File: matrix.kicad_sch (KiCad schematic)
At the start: 195 parts, among them SW10 ?, SW100 ?, SW101 ?, SW102 ?, SW103 ?, SW104 ?, SW105 ?, SW11 ?, SW12 ?, SW13 ?, SW14 ?, SW15 ?, SW16 ?, SW17 ?, SW18 ?, SW19 ?, SW2 ?, SW20 ?, SW21 ?, SW22 ?, SW23 ?, SW24 ?, SW25 ?, SW26 ?, SW27 ?, SW28 ?, SW29 ?, SW3 ?, SW30 ?, SW31 ?, SW32 ?, SW33 ?, SW34 ?, SW35 ?, SW36 ?, SW37 ?, SW38 ?, SW39 ?, SW4 ?, SW40 ?, SW41 ?, SW42 ?, SW43 ?, SW44 ?, SW45 ?, SW46 ?, SW47 ?, SW48 ?, SW49 ?, SW5 ?, SW50 ?, SW51 ?, SW52 ?, SW53 ?, SW54 ?, SW55 ?, SW56 ?, SW57 ?, SW58 ?, SW59 ?, SW6 ?, SW60 ?, SW61 ?, SW62 ?, SW63 ?, SW64 ?, SW65 ?, SW66 ?, SW67 ?, SW68 ?, SW69 ?, SW7 ?, SW70 ?, SW71 ?, SW72 ?, SW73 ?, SW74 ?, SW75 ?, SW76 ?, SW77 ?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

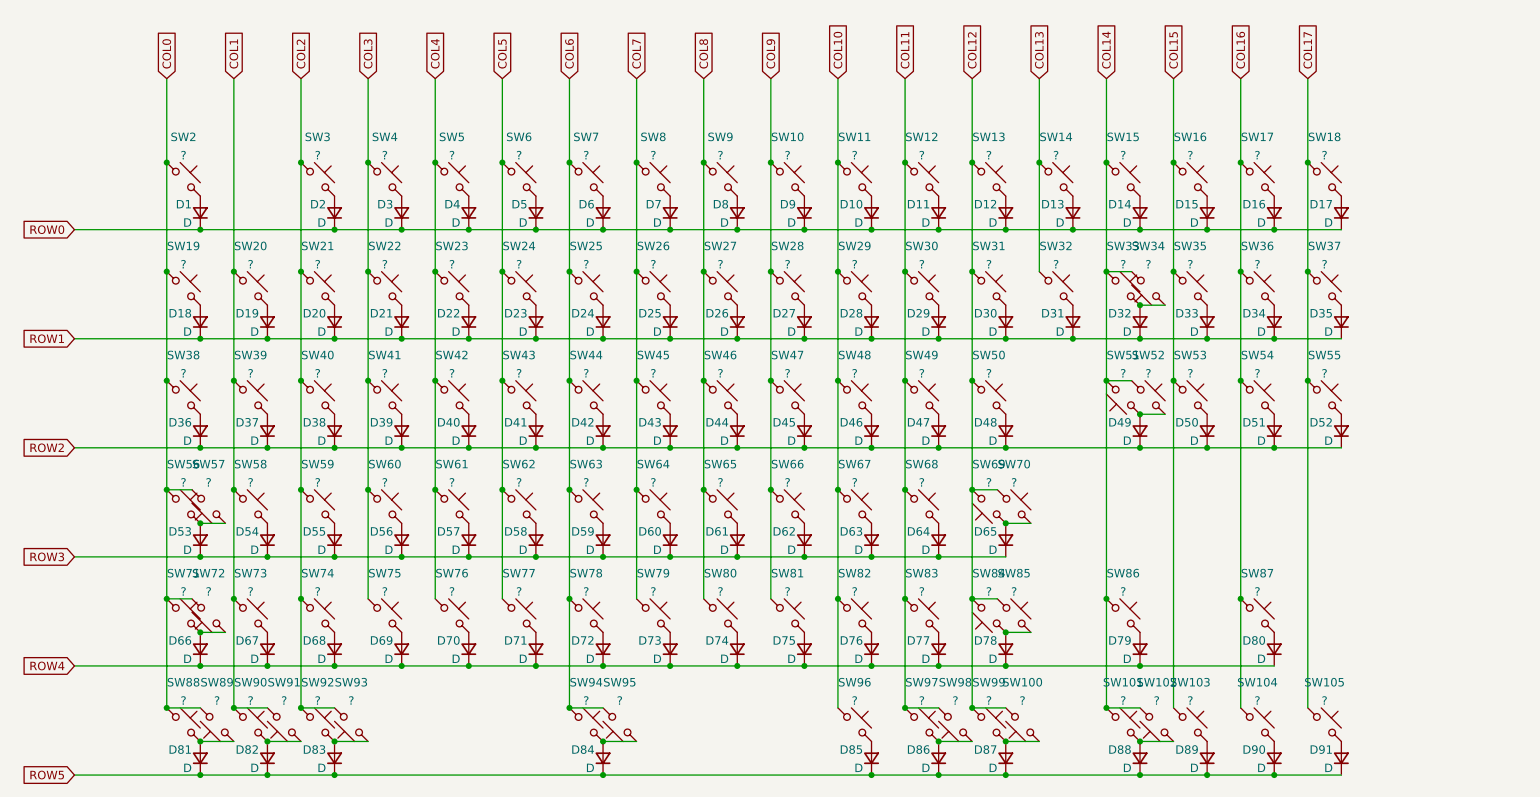
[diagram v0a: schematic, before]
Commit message: Added Stabilizers
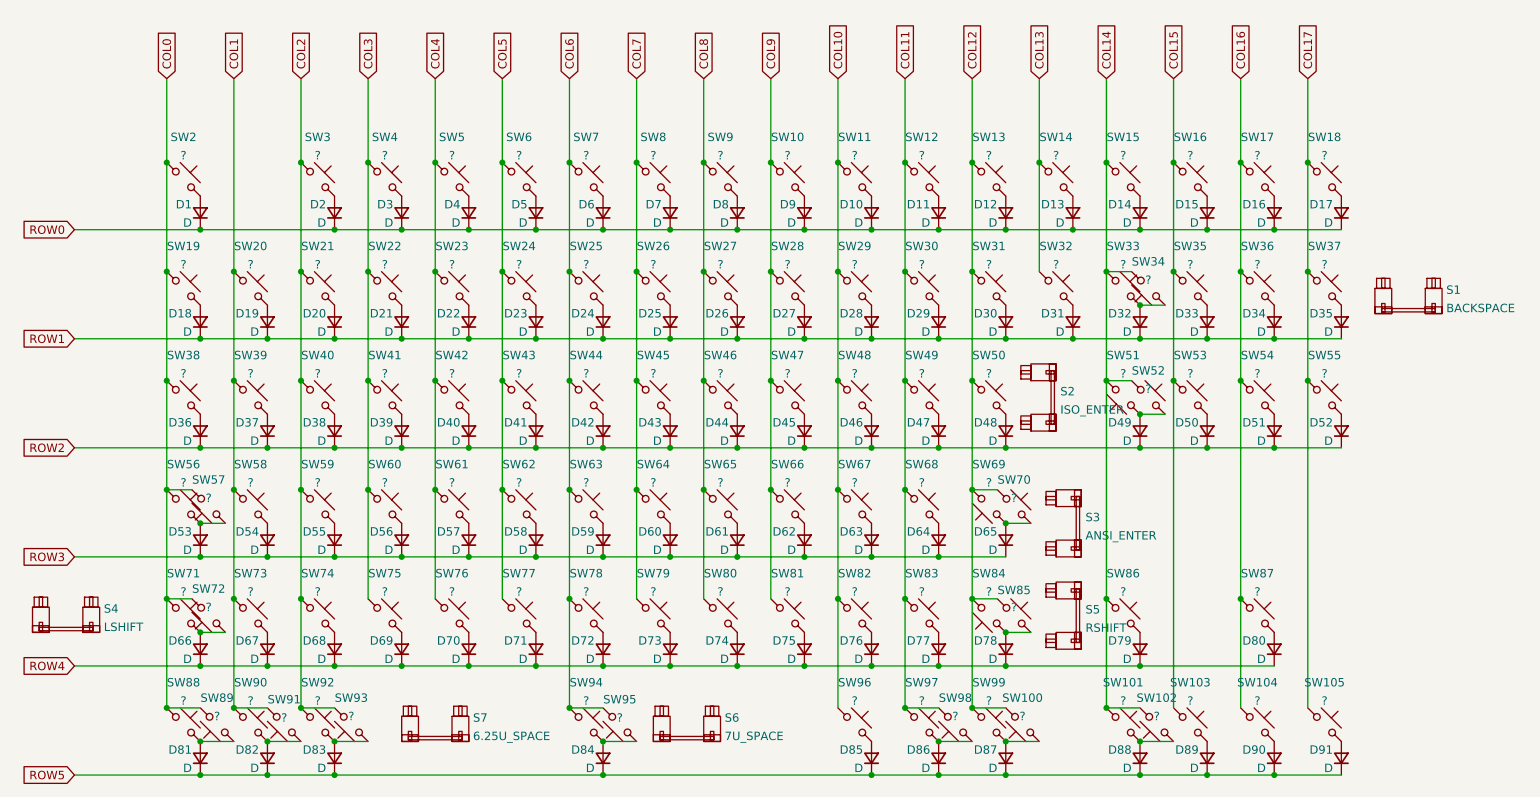
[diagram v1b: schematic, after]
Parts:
- added S1: BACKSPACE, marbastlib-mx:STAB_MX_2u, symbol marbastlib-mx:MX_stab
- added S2: ISO_ENTER, marbastlib-mx:STAB_MX_ISO_FLIPPED, symbol marbastlib-mx:MX_stab
- added S3: ANSI_ENTER, marbastlib-mx:STAB_MX_2.25u, symbol marbastlib-mx:MX_stab
- added S4: LSHIFT, marbastlib-mx:STAB_MX_2.25u, symbol marbastlib-mx:MX_stab
- added S5: RSHIFT, marbastlib-mx:STAB_MX_2.75u, symbol marbastlib-mx:MX_stab
- added S6: 7U_SPACE, marbastlib-mx:STAB_MX_7u, symbol marbastlib-mx:MX_stab
- added S7: 6.25U_SPACE, marbastlib-mx:STAB_MX_6.25u, symbol marbastlib-mx:MX_stab

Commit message: All switches (not diodes) in position
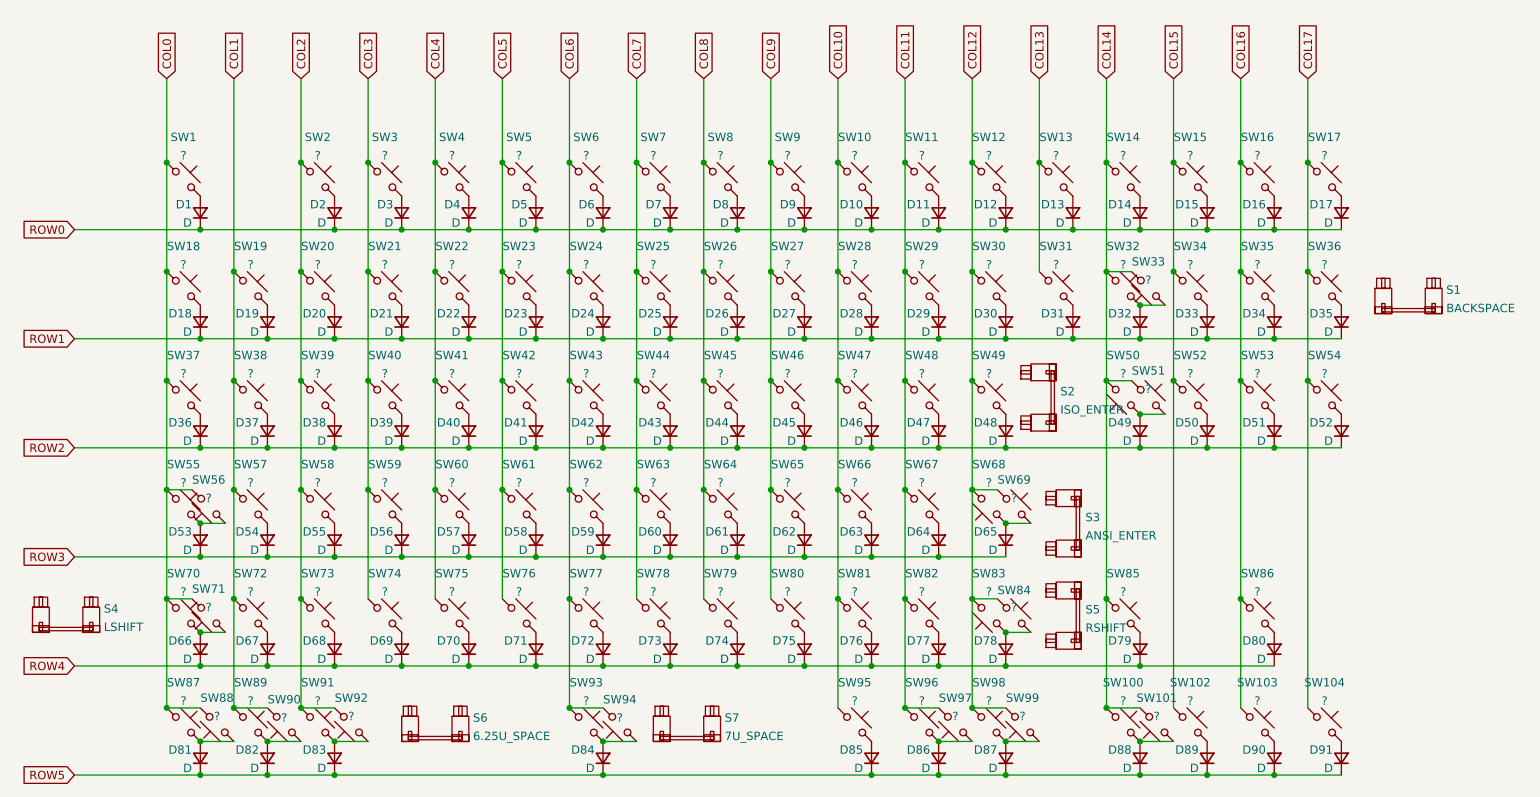
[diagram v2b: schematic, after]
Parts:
- renumbered S7 to S6, S6 to S7, SW2 to SW1, SW11 to SW10, SW101 to SW100, SW102 to SW101, SW103 to SW102, SW104 to SW103, SW105 to SW104, SW12 to SW11, SW13 to SW12, SW14 to SW13, SW15 to SW14, SW16 to SW15, SW17 to SW16, SW18 to SW17, SW19 to SW18, SW20 to SW19, SW3 to SW2, SW21 to SW20, SW22 to SW21, SW23 to SW22, SW24 to SW23, SW25 to SW24, SW26 to SW25, SW27 to SW26, SW28 to SW27, SW29 to SW28, SW30 to SW29, SW4 to SW3, SW31 to SW30, SW32 to SW31, SW33 to SW32, SW34 to SW33, SW35 to SW34, SW36 to SW35, SW37 to SW36, SW38 to SW37, SW39 to SW38, SW40 to SW39, SW5 to SW4, SW41 to SW40, SW42 to SW41, SW43 to SW42, SW44 to SW43, SW45 to SW44, SW46 to SW45, SW47 to SW46, SW48 to SW47, SW49 to SW48, SW50 to SW49, SW6 to SW5, SW51 to SW50, SW52 to SW51, SW53 to SW52, SW54 to SW53, SW55 to SW54, SW56 to SW55, SW57 to SW56, SW58 to SW57, SW59 to SW58, SW60 to SW59, SW7 to SW6, SW61 to SW60, SW62 to SW61, SW63 to SW62, SW64 to SW63, SW65 to SW64, SW66 to SW65, SW67 to SW66, SW68 to SW67, SW69 to SW68, SW70 to SW69, SW8 to SW7, SW71 to SW70, SW72 to SW71, SW73 to SW72, SW74 to SW73, SW75 to SW74, SW76 to SW75, SW77 to SW76, SW78 to SW77, SW79 to SW78, SW80 to SW79, SW9 to SW8, SW81 to SW80, SW82 to SW81, SW83 to SW82, SW84 to SW83, SW85 to SW84, SW86 to SW85, SW87 to SW86, SW88 to SW87, SW89 to SW88, SW90 to SW89, SW10 to SW9, SW91 to SW90, SW92 to SW91, SW93 to SW92, SW94 to SW93, SW95 to SW94, SW96 to SW95, SW97 to SW96, SW98 to SW97, SW99 to SW98, SW100 to SW99

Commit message: Changed Diodes to sod123
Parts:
- D1, D10, D11, D12, D13, D14, D15, D16, D17, D18, D19, D2, D20, D21, D22, D23, D24, D25, D26, D27, D28, D29, D3, D30, D31, D32, D33, D34, D35, D36, D37, D38, D39, D4, D40, D41, D42, D43, D44, D45, D46, D47, D48, D49, D5, D50, D51, D52, D53, D54, D55, D56, D57, D58, D59, D6, D60, D61, D62, D63, D64, D65, D66, D67, D68, D69, D7, D70, D71, D72, D73, D74, D75, D76, D77, D78, D79, D8, D80, D81, D82, D83, D84, D85, D86, D87, D88, D89, D9, D90, D91: footprint Diode_SMD:D_0402_1005Metric -> Diode_SMD:D_SOD-123
- SW100, SW37, SW50, SW88, SW92, SW96: footprint marbastlib-mx:SW_MX_HS_1u -> marbastlib-mx:SW_MX_HS_1.5u
- SW101, SW70, SW87, SW89, SW91, SW95, SW97, SW99: footprint marbastlib-mx:SW_MX_HS_1u -> marbastlib-mx:SW_MX_HS_1.25u
- SW55: footprint marbastlib-mx:SW_MX_HS_1u -> marbastlib-mx:SW_MX_HS_1.75u_stp
- SW56, SW83: footprint marbastlib-mx:SW_MX_HS_1u -> marbastlib-mx:SW_MX_HS_1.75u

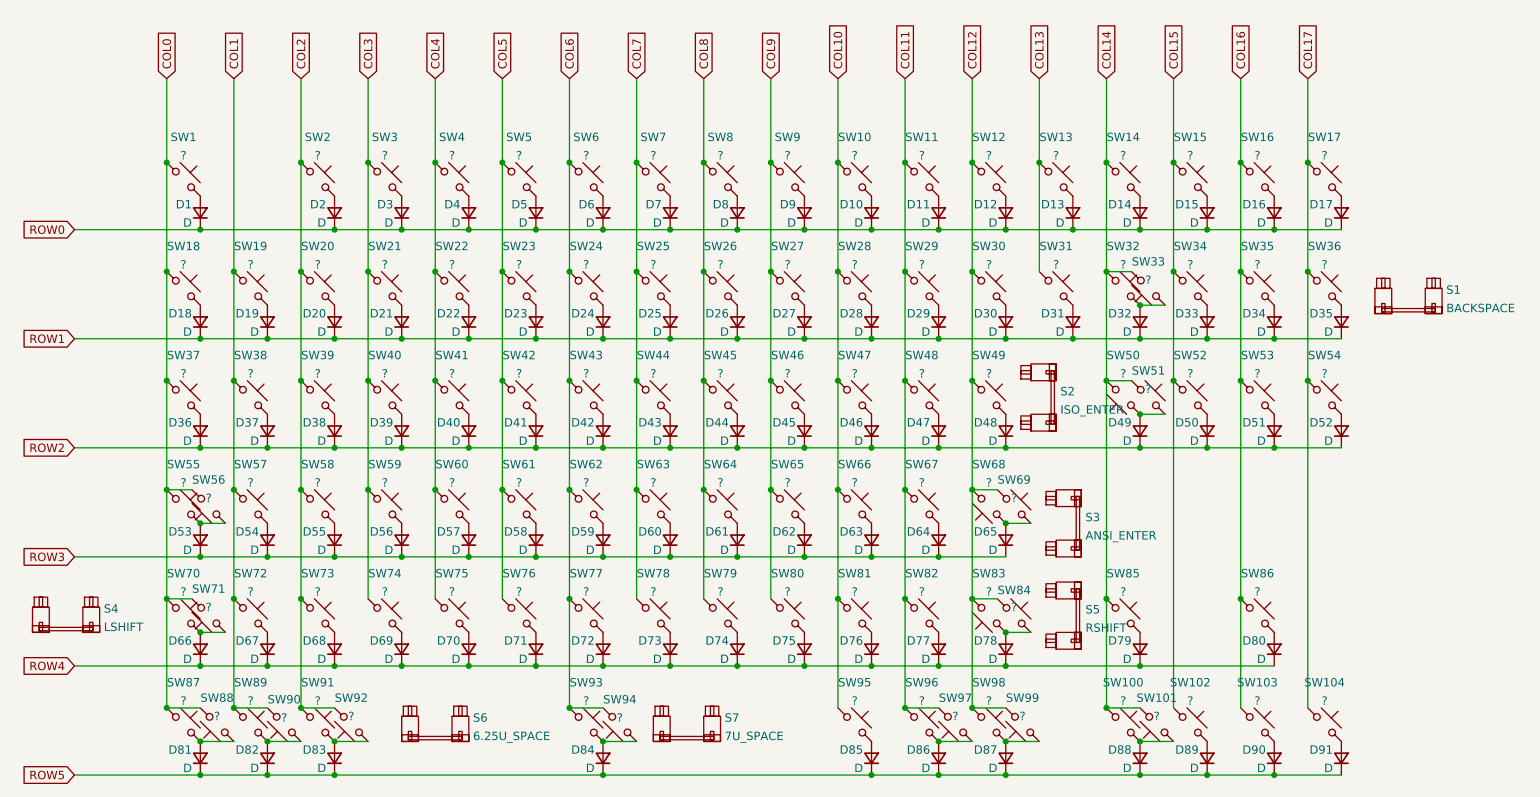
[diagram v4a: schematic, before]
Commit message: [Big changes] Added flex cuts and changed switch matrix/ pinout
- Optimized switch matrix by changing how the split backspace is done. It now connects to a different row instead of creating a whole different column
- Shifted a lot of traces/pins over by one, slight retracing work around the mcu area
- Added one more pin to the unused pins header
- Added 2 simple flex cuts
- Slight shifting around of different diodes
- Added 3d model for JST and USB-C Connector
- Extended bottom of the pcb by 0.5mm to accommodate for stab holes a bit better.
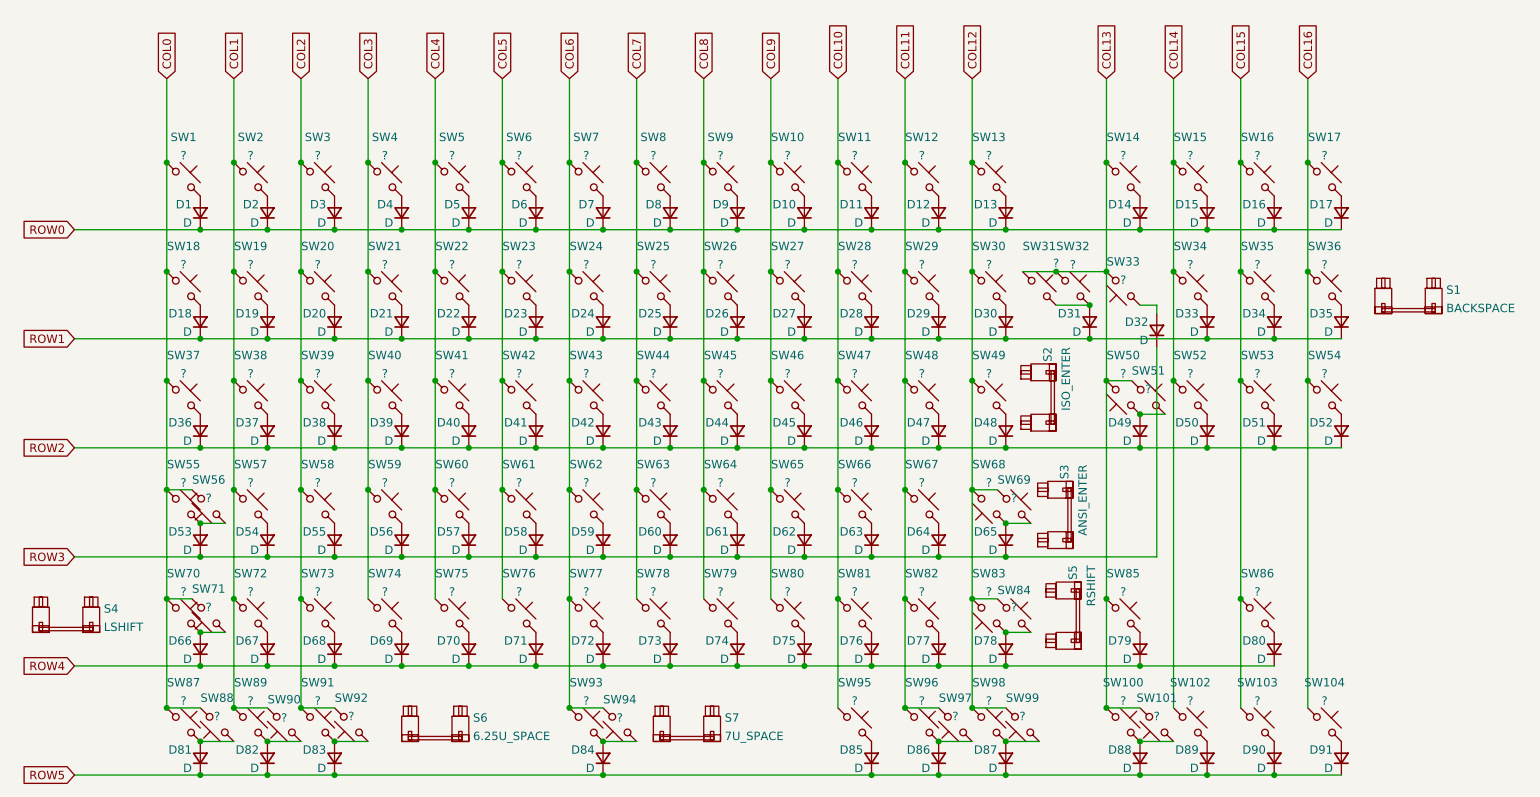
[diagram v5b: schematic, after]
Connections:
- net COL17 is gone; now on net COL16: SW104.1, SW17.1, SW36.1, SW54.1
- net COL1: now also SW2.1
- net COL10: now also SW11.1; no longer SW10.1
- net COL11: now also SW12.1; no longer SW11.1
- net COL12: now also SW13.1; no longer SW12.1
- net COL13: now also SW100.1, SW101.2, SW14.1, SW32.1, SW33.2, SW50.2, SW51.1, SW85.1; no longer SW13.1
- net COL14: now also SW102.1, SW15.1, SW34.1, SW52.1; no longer SW100.1, SW101.2, SW14.1, SW32.1, SW33.2, SW50.2, SW51.1, SW85.1
- net COL15: now also SW103.1, SW16.1, SW35.1, SW53.1, SW86.1; no longer SW102.1, SW15.1, SW34.1, SW52.1
- net COL16: no longer SW103.1, SW16.1, SW35.1, SW53.1, SW86.1
- net COL2: now also SW3.1; no longer SW2.1
- net COL3: now also SW4.1; no longer SW3.1
- net COL4: now also SW5.1; no longer SW4.1
- net COL5: now also SW6.1; no longer SW5.1
- net COL6: now also SW7.1; no longer SW6.1
- net COL7: now also SW8.1; no longer SW7.1
- net COL8: now also SW9.1; no longer SW8.1
- net COL9: now also SW10.1; no longer SW9.1
- net ROW1: no longer D32.1 (K)
- net ROW3: now also D32.1 (K)
- net at D31.2 (A), SW31.2: now also SW32.2
- net at D32.2 (A), SW33.1: no longer SW32.2
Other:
- moved on the sheet: D10, D11, D12, D13, D2, D3, D31, D32, D4, D5, D6, D7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

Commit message: Updated BOM inclusions
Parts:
- S1, S2, S3, S4, S5, S6, S7: now left out of the parts list
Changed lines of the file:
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@@
   )
   (symbol (lib_id "marbastlib-mx:MX_stab") (at 243.84 69.85 0) (unit 1)
-    (in_bom yes) (on_board yes) (fields_autoplaced)
+    (in_bom no) (on_board yes) (fields_autoplaced)
     (property "Reference" "S1" (id 0) (at 249.555 68.8145 0)
       (effects (font (size 1.27 1.27)) (justify left))
@@
   )
   (symbol (lib_id "marbastlib-mx:MX_stab") (at 191.77 118.11 90) (unit 1)
-    (in_bom yes) (on_board yes)
+    (in_bom no) (on_board yes)
     (property "Reference" "S5" (id 0) (at 193.04 110.49 0)
       (effects (font (size 1.27 1.27)) (justify right))
@@
   )
   (symbol (lib_id "marbastlib-mx:MX_stab") (at 187.96 85.09 90) (unit 1)
-    (in_bom yes) (on_board yes)
+    (in_bom no) (on_board yes)
     (property "Reference" "S2" (id 0) (at 189.23 77.47 0)
       (effects (font (size 1.27 1.27)) (justify right))
@@
   )
   (symbol (lib_id "marbastlib-mx:MX_stab") (at 134.62 134.62 0) (unit 1)
-    (in_bom yes) (on_board yes) (fields_autoplaced)
+    (in_bom no) (on_board yes) (fields_autoplaced)
     (property "Reference" "S7" (id 0) (at 140.335 133.5845 0)
       (effects (font (size 1.27 1.27)) (justify left))
@@
   )
   (symbol (lib_id "marbastlib-mx:MX_stab") (at 190.5 102.87 90) (unit 1)
-    (in_bom yes) (on_board yes)
+    (in_bom no) (on_board yes)
     (property "Reference" "S3" (id 0) (at 191.77 95.25 0)
       (effects (font (size 1.27 1.27)) (justify right))
@@
   )
   (symbol (lib_id "marbastlib-mx:MX_stab") (at 40.64 118.11 0) (unit 1)
-    (in_bom yes) (on_board yes) (fields_autoplaced)
+    (in_bom no) (on_board yes) (fields_autoplaced)
     (property "Reference" "S4" (id 0) (at 46.355 117.0745 0)
       (effects (font (size 1.27 1.27)) (justify left))
@@
   )
   (symbol (lib_id "marbastlib-mx:MX_stab") (at 96.52 134.62 0) (unit 1)
-    (in_bom yes) (on_board yes) (fields_autoplaced)
+    (in_bom no) (on_board yes) (fields_autoplaced)
     (property "Reference" "S6" (id 0) (at 102.235 133.5845 0)
       (effects (font (size 1.27 1.27)) (justify left))

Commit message: Generated manufacturing files (JLC), Updated Sleep-lib to a submodule, updated manufacturing files/part numbers
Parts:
- SW1, SW10, SW100, SW101, SW102, SW103, SW104, SW11, SW12, SW13, SW14, SW15, SW16, SW17, SW18, SW19, SW2, SW20, SW21, SW22, SW23, SW24, SW25, SW26, SW27, SW28, SW29, SW3, SW30, SW31, SW32, SW33, SW34, SW35, SW36, SW37, SW38, SW39, SW4, SW40, SW41, SW42, SW43, SW44, SW45, SW46, SW47, SW48, SW49, SW5, SW50, SW51, SW52, SW53, SW54, SW55, SW56, SW57, SW58, SW59, SW6, SW60, SW61, SW62, SW63, SW64, SW65, SW66, SW67, SW68, SW69, SW7, SW70, SW71, SW72, SW73, SW74, SW75, SW76, SW77, SW78, SW79, SW8, SW80, SW81, SW82, SW83, SW84, SW85, SW86, SW87, SW88, SW89, SW9, SW90, SW91, SW92, SW93, SW94, SW95, SW96, SW97, SW98, SW99: LCSC (none) -> C5156480
